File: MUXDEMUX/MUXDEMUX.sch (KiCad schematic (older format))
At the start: 21 parts, among them SW1 SW_DIP_x08, U1 74LS86, U2 74138, U3 74LS86, U4 74151, U5 74LS04

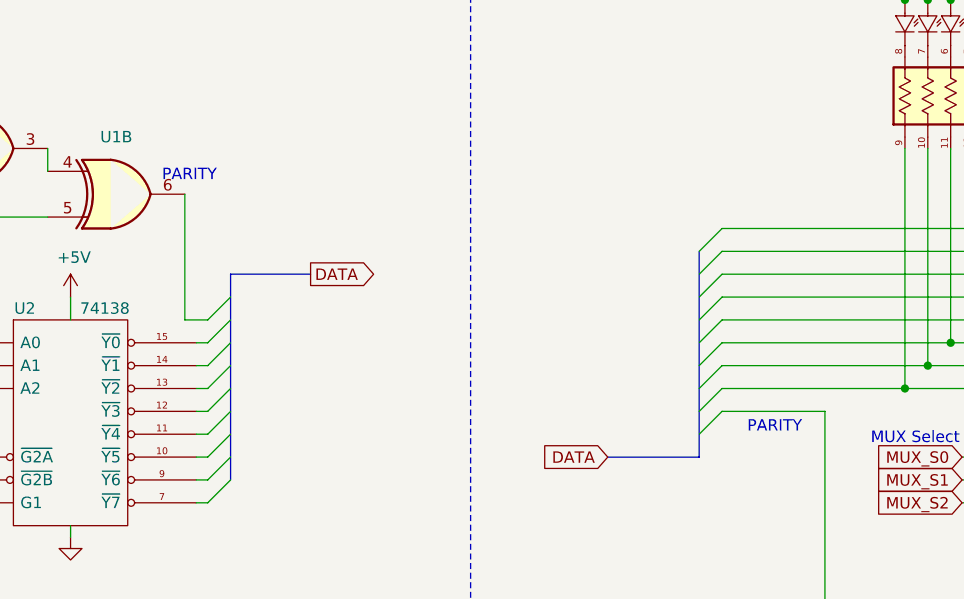
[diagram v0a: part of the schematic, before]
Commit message: fix parity bit label
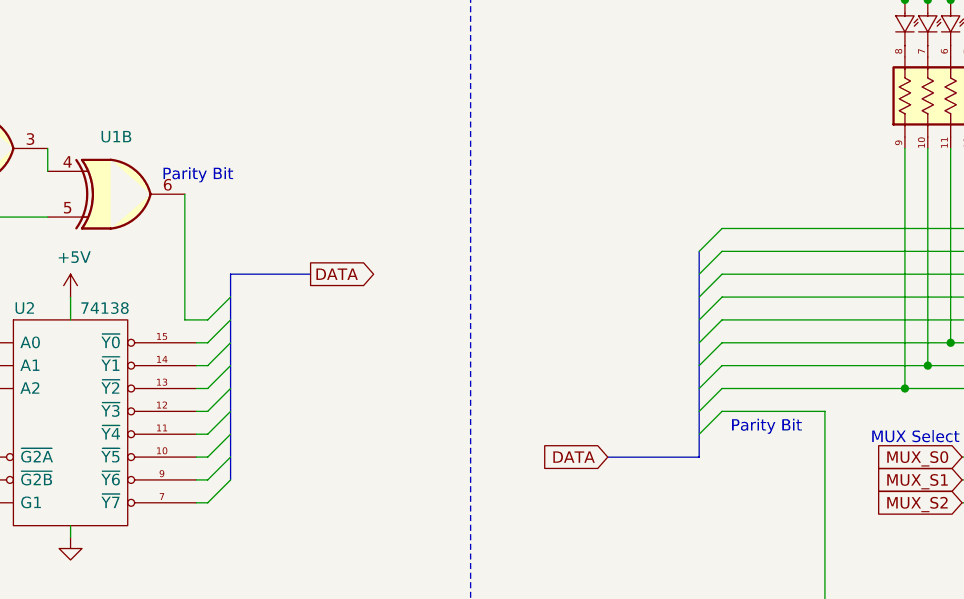
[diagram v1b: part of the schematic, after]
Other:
- note added: "Parity Bit"
- note removed: "PARITY"
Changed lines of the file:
@@
 	3300 2050 3650 2050
 Text Notes 3000 1650 0    50   ~ 0
-PARITY
+Parity Bit
 Wire Wire Line
 	8100 3900 8100 4000
@@
 Address\nError
 Text Notes 5800 2750 2    50   ~ 0
-PARITY
+Parity Bit
 Wire Wire Line
 	2050 3050 1700 3050

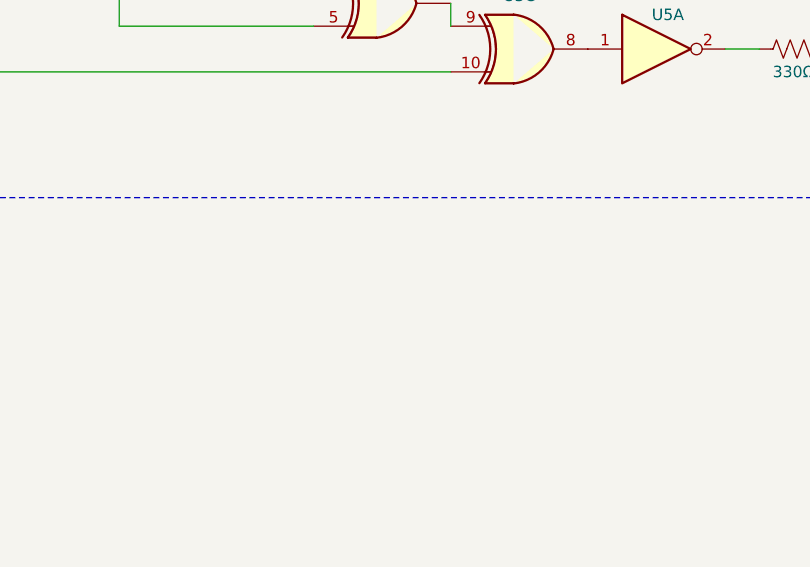
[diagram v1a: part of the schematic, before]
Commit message: add important diode
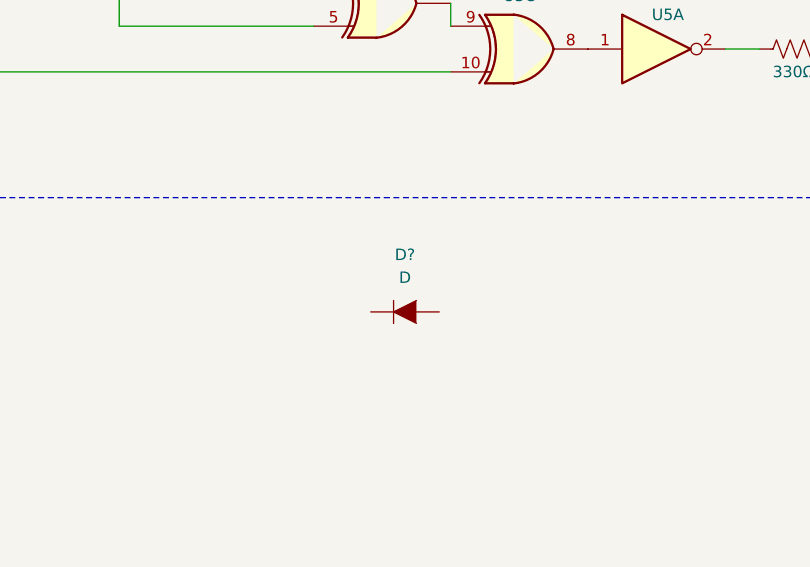
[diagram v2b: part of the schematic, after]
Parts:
- added D?: D, symbol 00TJR:D
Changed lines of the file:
@@
 Wire Bus Line
 	5350 1950 5350 2850
+$Comp
+L 00TJR:D D?
+U 1 1 5FA071EB
+P 7900 5250
+F 0 "D?" H 7900 5500 50  0000 C CNN
+F 1 "D" H 7900 5400 50  0000 C CNN
+F 2 "" H 7900 5250 50  0000 C CNN
+F 3 "" H 7900 5250 50  0000 C CNN
+	1    7900 5250
+	1    0    0    -1
+$EndComp
 $EndSCHEMATC
